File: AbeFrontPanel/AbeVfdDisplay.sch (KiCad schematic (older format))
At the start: 21 parts

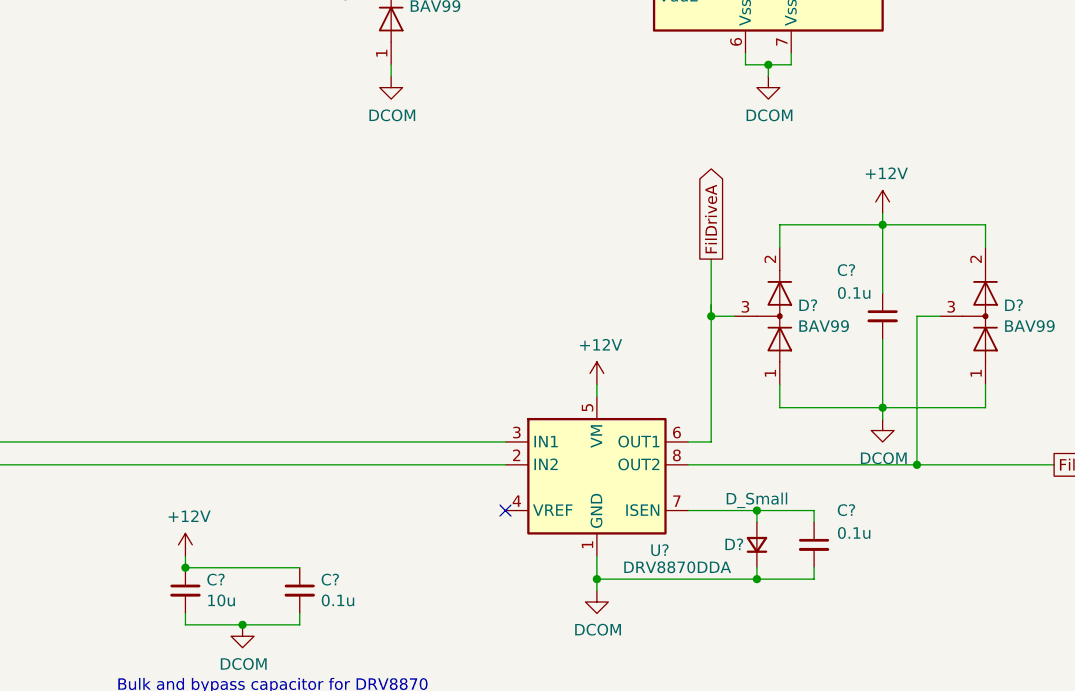
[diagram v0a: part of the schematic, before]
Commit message: +10V, Beeper
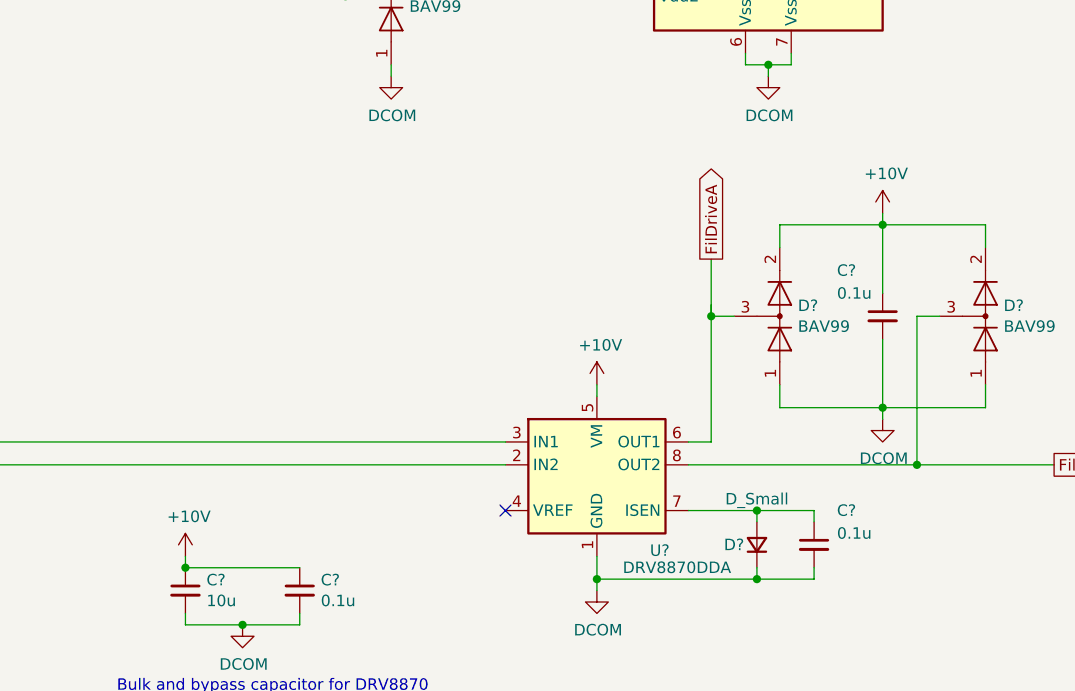
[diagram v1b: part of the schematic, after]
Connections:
- net +12V renamed +10V
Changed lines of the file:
@@
-	1    0    0    -1
-$EndComp
-$Comp
-L power:+12V #PWR?
-U 1 1 60CCC2D4
-P 3400 6050
-F 0 "#PWR?" H 3400 5900 50  0001 C CNN
-F 1 "+12V" H 3415 6223 50  0000 C CNN
-F 2 "" H 3400 6050 50  0001 C CNN
-F 3 "" H 3400 6050 50  0001 C CNN
-	1    3400 6050
 	1    0    0    -1
 $EndComp
@@
 Wire Wire Line
 	6450 4600 6450 4550
-$Comp
-L power:+12V #PWR?
-U 1 1 60CFAD3C
-P 6450 4550
-F 0 "#PWR?" H 6450 4400 50  0001 C CNN
-F 1 "+12V" H 6465 4723 50  0000 C CNN
-F 2 "" H 6450 4550 50  0001 C CNN
-F 3 "" H 6450 4550 50  0001 C CNN
-	1    6450 4550
-	1    0    0    -1
-$EndComp
 Wire Wire Line
 	6900 4600 6900 4700
@@
 	5200 5350 5200 5300
 $Comp
-L power:+12V #PWR?
-U 1 1 60CCB3E7
-P 5200 5300
-F 0 "#PWR?" H 5200 5150 50  0001 C CNN
-F 1 "+12V" H 5215 5473 50  0000 C CNN
-F 2 "" H 5200 5300 50  0001 C CNN
-F 3 "" H 5200 5300 50  0001 C CNN
-	1    5200 5300
-	1    0    0    -1
-$EndComp
-$Comp
 L Driver_Motor:DRV8870DDA U?
 U 1 1 60CBD48A
@@
 Wire Wire Line
 	900  7200 900  7100
+$Comp
+L power:+10V #PWR?
+U 1 1 60BFD5E5
+P 5200 5300
+F 0 "#PWR?" H 5200 5150 50  0001 C CNN
+F 1 "+10V" H 5215 5473 50  0000 C CNN
+F 2 "" H 5200 5300 50  0001 C CNN
+F 3 "" H 5200 5300 50  0001 C CNN
+	1    5200 5300
+	1    0    0    -1
+$EndComp
+$Comp
+L power:+10V #PWR?
+U 1 1 60C08807
+P 6450 4550
+F 0 "#PWR?" H 6450 4400 50  0001 C CNN
+F 1 "+10V" H 6465 4723 50  0000 C CNN
+F 2 "" H 6450 4550 50  0001 C CNN
+F 3 "" H 6450 4550 50  0001 C CNN
+	1    6450 4550
+	1    0    0    -1
+$EndComp
+$Comp
+L power:+10V #PWR?
+U 1 1 60C08D2F
+P 3400 6050
+F 0 "#PWR?" H 3400 5900 50  0001 C CNN
+F 1 "+10V" H 3415 6223 50  0000 C CNN
+F 2 "" H 3400 6050 50  0001 C CNN
+F 3 "" H 3400 6050 50  0001 C CNN
+	1    3400 6050
+	1    0    0    -1
+$EndComp
 $EndSCHEMATC

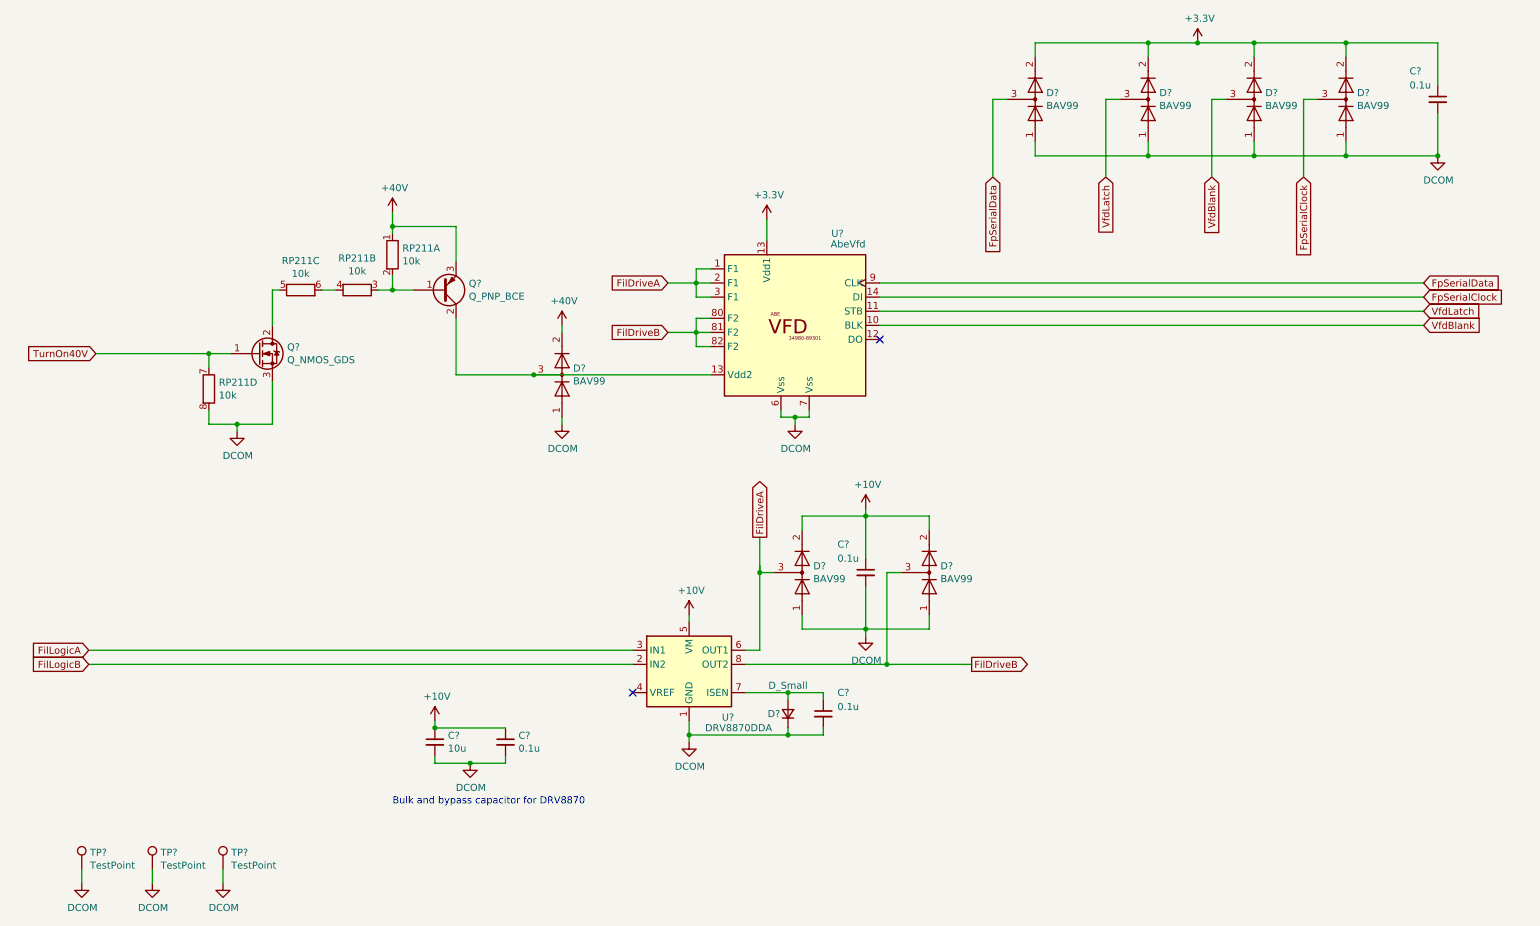
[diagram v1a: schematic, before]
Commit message: Add RC time constant to slow down FilLogic. Add DRV8210 symbol.
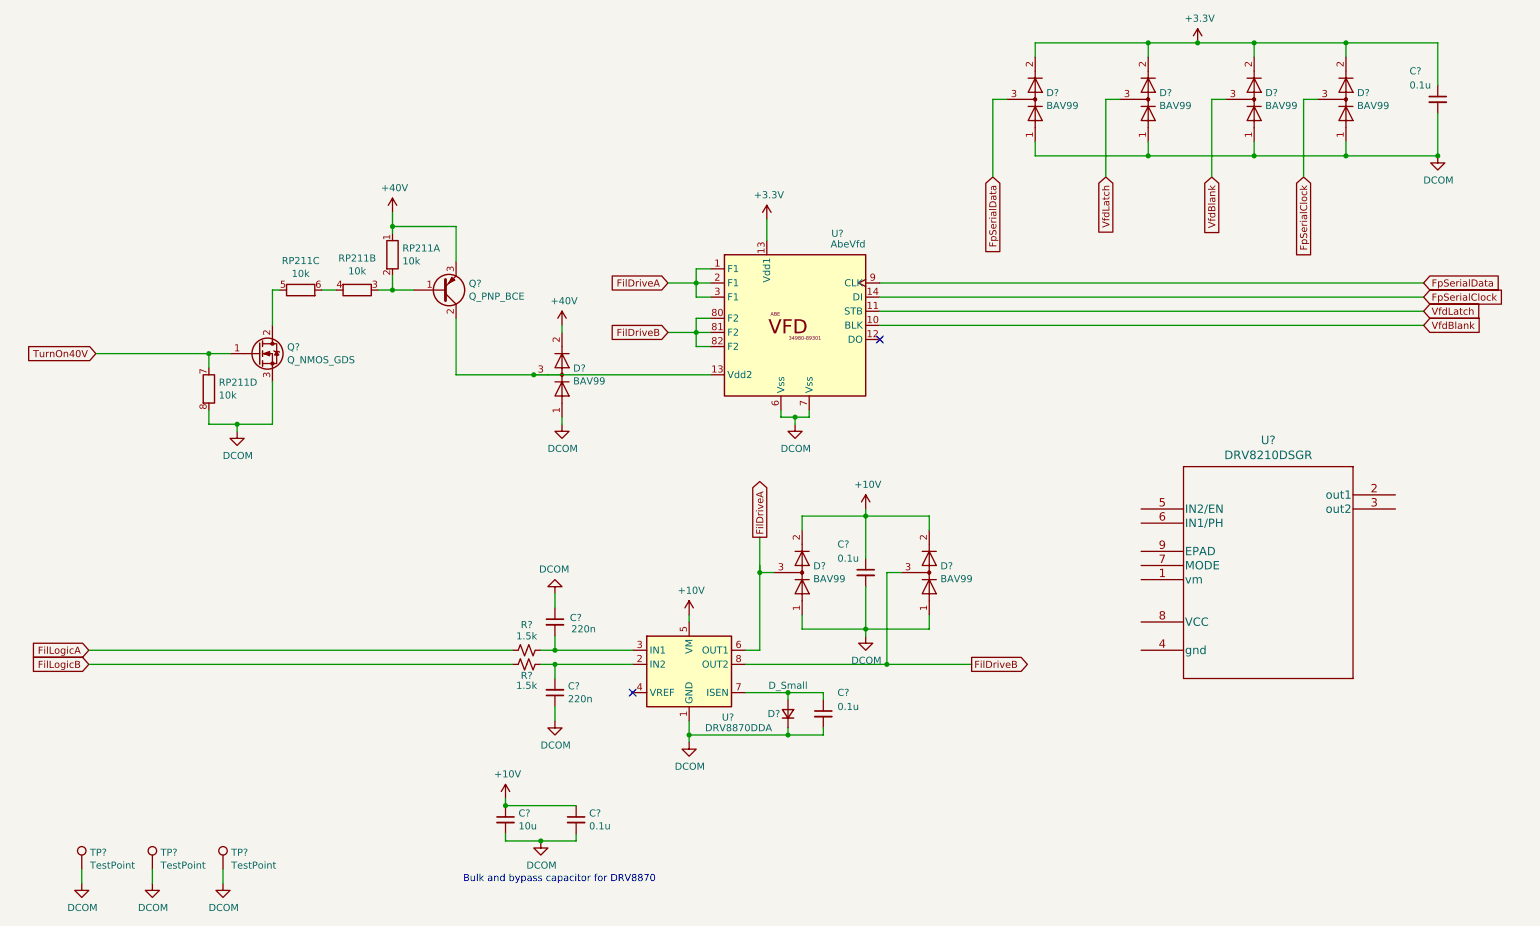
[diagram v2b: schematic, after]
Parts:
- added C? (x2): 220n, symbol Device:C_Small
- added R? (x2): 1.5k, symbol Device:R_Small_US
- added U?: DRV8210DSGR, WSON08_2X2_TEX, symbol DRV8210DSGR:DRV8210DSGR
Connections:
- net FilLogicA: now also R?.1; no longer U?.3 (IN1)
- net FilLogicB: now also R?.2; no longer U?.2 (IN2)
- net GND: now also C?.1, C?.1
- new net: C?.2, R?.1, U?.2 (IN2)
- new net: C?.2, R?.2, U?.3 (IN1)
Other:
- moved on the sheet: C?
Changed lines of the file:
@@
 Wire Wire Line
 	6550 3250 10400 3250
-Text Notes 3100 6650 0    50   ~ 0
+Text Notes 3600 7200 0    50   ~ 0
 Bulk and bypass capacitor for DRV8870\n
 Wire Wire Line
-	3900 6350 3900 6300
-Wire Wire Line
-	3400 6300 3400 6350
-Connection ~ 3400 6100
-Wire Wire Line
-	3400 6050 3400 6100
-Wire Wire Line
-	3900 6100 3400 6100
+	4400 6900 4400 6850
+Wire Wire Line
+	3900 6850 3900 6900
+Connection ~ 3900 6650
+Wire Wire Line
+	3900 6600 3900 6650
+Wire Wire Line
+	4400 6650 3900 6650
 $Comp
 L Device:C_Small C?
 U 1 1 60CCDCB6
-P 3900 6200
-F 0 "C?" H 3992 6246 50  0000 L CNN
-F 1 "0.1u" H 3992 6155 50  0000 L CNN
-F 2 "" H 3900 6200 50  0001 C CNN
-F 3 "~" H 3900 6200 50  0001 C CNN
-	1    3900 6200
+P 4400 6750
+F 0 "C?" H 4492 6796 50  0000 L CNN
+F 1 "0.1u" H 4492 6705 50  0000 L CNN
+F 2 "" H 4400 6750 50  0001 C CNN
+F 3 "~" H 4400 6750 50  0001 C CNN
+	1    4400 6750
 	1    0    0    -1
 $EndComp
@@
 L Device:C_Small C?
 U 1 1 60CCD608
-P 3400 6200
-F 0 "C?" H 3492 6246 50  0000 L CNN
-F 1 "10u" H 3492 6155 50  0000 L CNN
-F 2 "" H 3400 6200 50  0001 C CNN
-F 3 "~" H 3400 6200 50  0001 C CNN
-	1    3400 6200
-	1    0    0    -1
-$EndComp
-Wire Wire Line
-	4800 5650 950  5650
-Wire Wire Line
-	950  5550 4800 5550
+P 3900 6750
+F 0 "C?" H 3992 6796 50  0000 L CNN
+F 1 "10u" H 3992 6705 50  0000 L CNN
+F 2 "" H 3900 6750 50  0001 C CNN
+F 3 "~" H 3900 6750 50  0001 C CNN
+	1    3900 6750
+	1    0    0    -1
+$EndComp
 Wire Wire Line
 	7350 1650 7450 1650
@@
 $EndComp
 Wire Wire Line
-	3400 6350 3650 6350
+	3900 6900 4150 6900
 $Comp
 L power:DCOM #PWR?
 U 1 1 6089038E
-P 3650 6350
-F 0 "#PWR?" H 3650 6100 50  0001 C CNN
-F 1 "DCOM" H 3655 6177 50  0000 C CNN
-F 2 "" H 3650 6350 50  0001 C CNN
-F 3 "" H 3650 6350 50  0001 C CNN
-	1    3650 6350
-	1    0    0    -1
-$EndComp
-Connection ~ 3650 6350
-Wire Wire Line
-	3650 6350 3900 6350
+P 4150 6900
+F 0 "#PWR?" H 4150 6650 50  0001 C CNN
+F 1 "DCOM" H 4155 6727 50  0000 C CNN
+F 2 "" H 4150 6900 50  0001 C CNN
+F 3 "" H 4150 6900 50  0001 C CNN
+	1    4150 6900
+	1    0    0    -1
+$EndComp
+Connection ~ 4150 6900
+Wire Wire Line
+	4150 6900 4400 6900
 $Comp
 L power:DCOM #PWR?
@@
 L power:+10V #PWR?
 U 1 1 60C08D2F
-P 3400 6050
-F 0 "#PWR?" H 3400 5900 50  0001 C CNN
-F 1 "+10V" H 3415 6223 50  0000 C CNN
-F 2 "" H 3400 6050 50  0001 C CNN
-F 3 "" H 3400 6050 50  0001 C CNN
-	1    3400 6050
-	1    0    0    -1
-$EndComp
+P 3900 6600
+F 0 "#PWR?" H 3900 6450 50  0001 C CNN
+F 1 "+10V" H 3915 6773 50  0000 C CNN
+F 2 "" H 3900 6600 50  0001 C CNN
+F 3 "" H 3900 6600 50  0001 C CNN
+	1    3900 6600
+	1    0    0    -1
+$EndComp
+$Comp
+L Device:R_Small_US R?
+U 1 1 60A61140
+P 4050 5650
+F 0 "R?" V 4130 5650 50  0000 C CNN
+F 1 "1.5k" V 4200 5650 50  0000 C CNN
+F 2 "" H 4050 5650 50  0001 C CNN
+F 3 "~" H 4050 5650 50  0001 C CNN
+	1    4050 5650
+	0    1    1    0
+$EndComp
+$Comp
+L Device:C_Small C?
+U 1 1 60A62089
+P 4250 5850
+F 0 "C?" H 4158 5804 50  0000 R CNN
+F 1 "220n" H 4158 5895 50  0000 R CNN
+F 2 "" H 4250 5850 50  0001 C CNN
+F 3 "~" H 4250 5850 50  0001 C CNN
+	1    4250 5850
+	-1   0    0    1
+$EndComp
+Wire Wire Line
+	4150 5650 4250 5650
+Wire Wire Line
+	4250 5650 4250 5750
+Wire Wire Line
+	4250 5650 4800 5650
+Connection ~ 4250 5650
+Wire Wire Line
+	3950 5650 950  5650
+$Comp
+L Device:R_Small_US R?
+U 1 1 60A73762
+P 4050 5550
+F 0 "R?" V 4230 5550 50  0000 C CNN
+F 1 "1.5k" V 4150 5550 50  0000 C CNN
+F 2 "" H 4050 5550 50  0001 C CNN
+F 3 "~" H 4050 5550 50  0001 C CNN
+	1    4050 5550
+	0    -1   -1   0
+$EndComp
+$Comp
+L Device:C_Small C?
+U 1 1 60A73AF6
+P 4250 5350
+F 0 "C?" H 4440 5380 50  0000 R CNN
+F 1 "220n" H 4540 5300 50  0000 R CNN
+F 2 "" H 4250 5350 50  0001 C CNN
+F 3 "~" H 4250 5350 50  0001 C CNN
+	1    4250 5350
+	1    0    0    -1
+$EndComp
+Wire Wire Line
+	4250 5550 4250 5450
+Wire Wire Line
+	4150 5550 4250 5550
+Wire Wire Line
+	4800 5550 4250 5550
+Connection ~ 4250 5550
+$Comp
+L power:DCOM #PWR?
+U 1 1 60A8A5B2
+P 4250 6050
+F 0 "#PWR?" H 4250 5800 50  0001 C CNN
+F 1 "DCOM" H 4255 5877 50  0000 C CNN
+F 2 "" H 4250 6050 50  0001 C CNN
+F 3 "" H 4250 6050 50  0001 C CNN
+	1    4250 6050
+	1    0    0    -1
+$EndComp
+$Comp
+L power:DCOM #PWR?
+U 1 1 60A8B484
+P 4250 5150
+F 0 "#PWR?" H 4250 4900 50  0001 C CNN
+F 1 "DCOM" H 4255 4977 50  0000 C CNN
+F 2 "" H 4250 5150 50  0001 C CNN
+F 3 "" H 4250 5150 50  0001 C CNN
+	1    4250 5150
+	-1   0    0    1
+$EndComp
+Wire Wire Line
+	4250 5150 4250 5250
+Wire Wire Line
+	4250 5950 4250 6050
+Wire Wire Line
+	3950 5550 950  5550
+$Comp
+L DRV8210DSGR:DRV8210DSGR U?
+U 1 1 60AAF839
+P 8400 4550
+F 0 "U?" H 9300 5037 60  0000 C CNN
+F 1 "DRV8210DSGR" H 9300 4931 60  0000 C CNN
+F 2 "WSON08_2X2_TEX" H 9300 4890 60  0001 C CNN
+F 3 "" H 8400 4550 60  0000 C CNN
+	1    8400 4550
+	1    0    0    -1
+$EndComp
